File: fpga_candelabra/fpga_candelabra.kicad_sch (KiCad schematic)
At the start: 6 parts

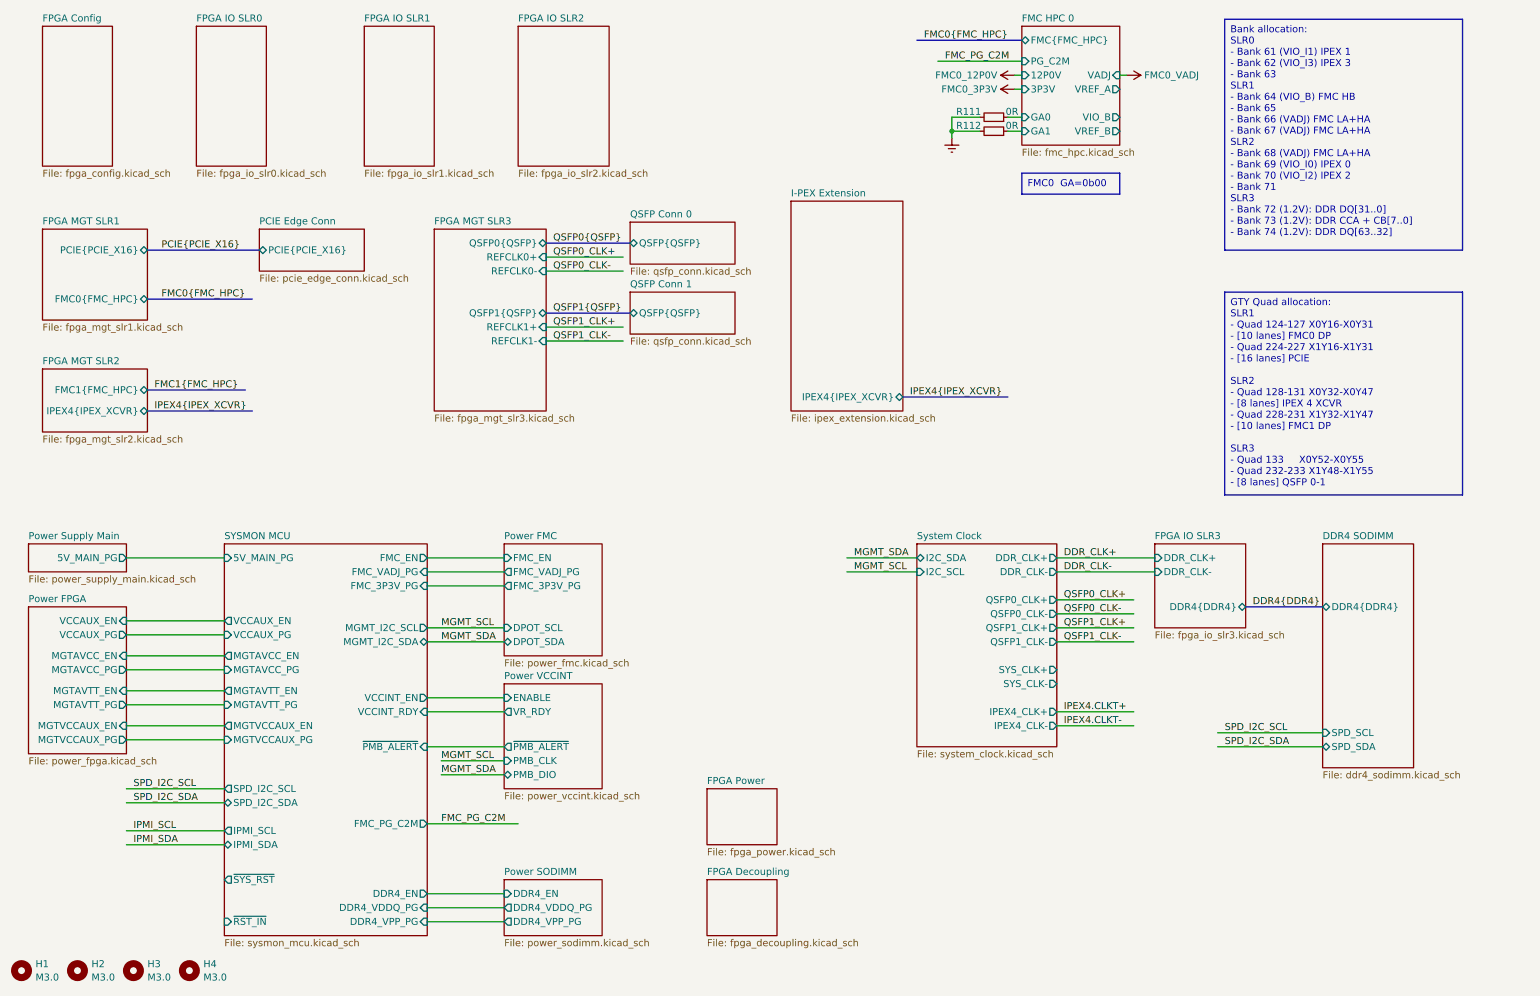
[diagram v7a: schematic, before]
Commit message: fpga_candelabra: major revision
* Finish DDR4 & QSFP+ & PCIe layout
* Change FMC to LPC
* Add mikroBUS extension
* 12V input & PDN updates
* FPGA config updates

Signed-off-by: Yichuan Gao <gaoyichuan000@gmail.com>
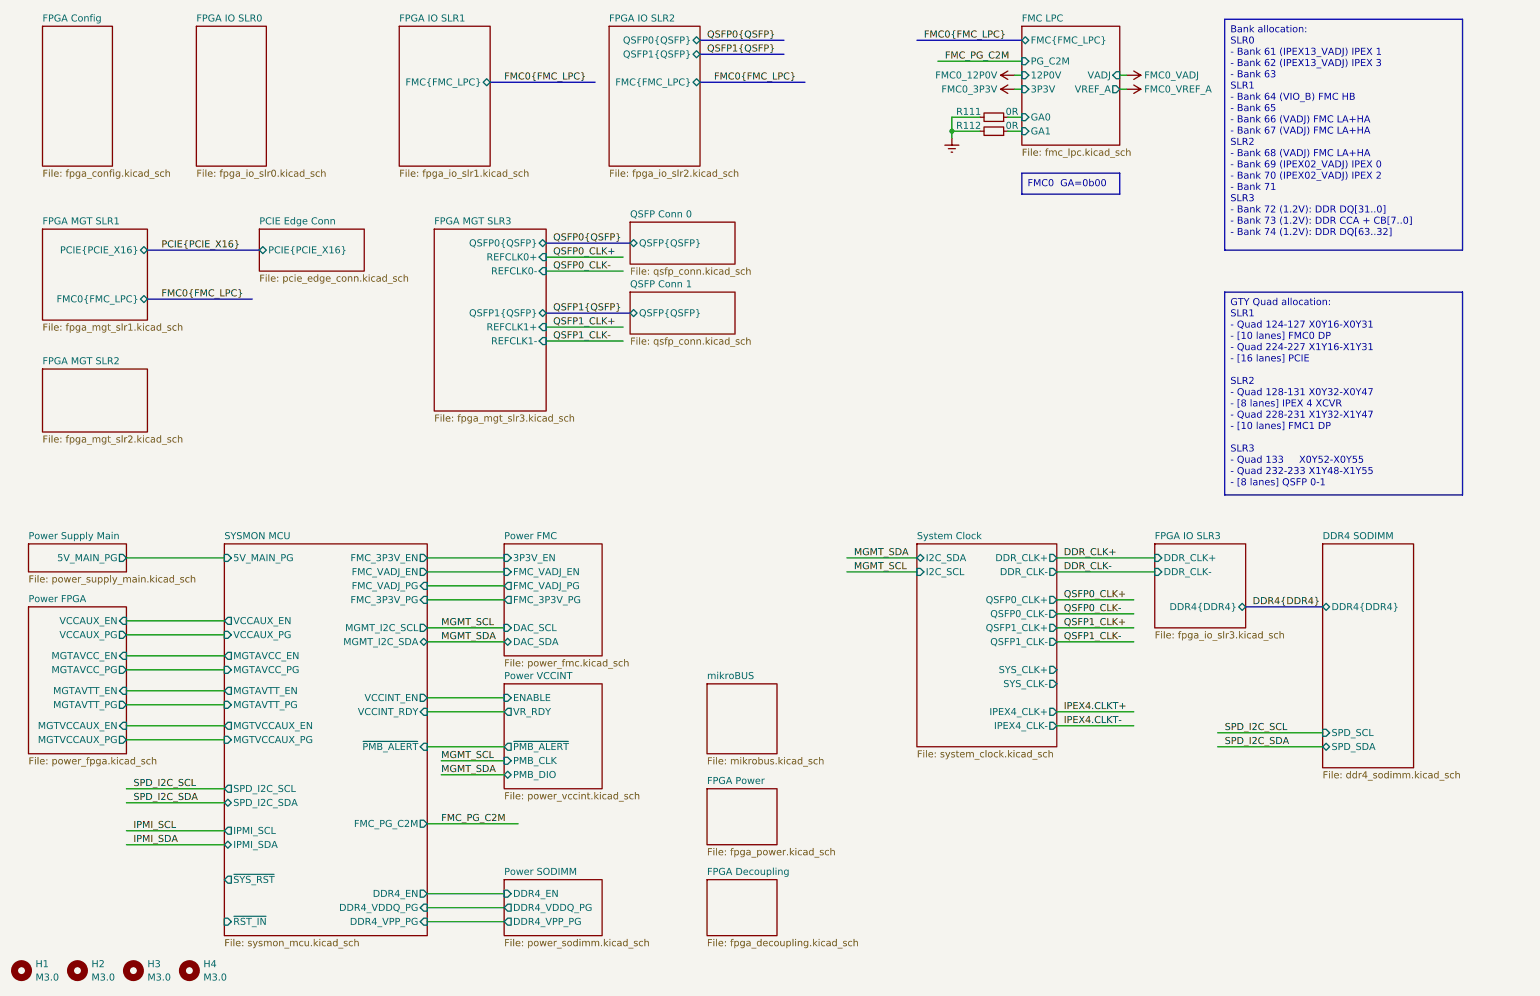
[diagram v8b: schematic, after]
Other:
- sheet FMC HPC 0 renamed FMC LPC
- removed sheet I-PEX Extension
- added sheet mikroBUS (mikrobus.kicad_sch)
- sheet FMC LPC: file fmc_hpc.kicad_sch -> fmc_lpc.kicad_sch
- sheet FMC LPC ports: added FMC{FMC_LPC}; removed FMC{FMC_HPC}, VIO_B, VREF_B
- sheet FPGA IO SLR1 ports: added FMC{FMC_LPC}; removed none
- sheet FPGA IO SLR2 ports: added FMC{FMC_LPC}, QSFP0{QSFP}, QSFP1{QSFP}; removed none
- sheet FPGA MGT SLR1 ports: added FMC0{FMC_LPC}; removed FMC0{FMC_HPC}
- sheet FPGA MGT SLR2 ports: added none; removed FMC1{FMC_HPC}, IPEX4{IPEX_XCVR}
- sheet Power FMC ports: added 3P3V_EN, DAC_SCL, DAC_SDA, FMC_VADJ_EN; removed DPOT_SCL, DPOT_SDA, FMC_EN
- sheet SYSMON MCU ports: added FMC_3P3V_EN, FMC_VADJ_EN; removed FMC_EN
